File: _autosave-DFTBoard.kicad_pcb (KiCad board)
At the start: 8 copper layers, 120 x 58 mm, 287 parts, among them CON1 AVR-JTAG-10, J1 PJ-102A, J2 AUDIO JACK, J3 AUDIO JACK, J4 AUDIO JACK, J5 JACK_TRS_4PINS, J6 USB_A, J7 USB_B, J8 Micro_SD_Card_Det, J9 HDMI_A, Q1 IRLML2502, Q10 IRLML2502, Q2 IRLML2502, Q3 IRLML2502, Q4 IRLML2502, Q5 IRLML2502, Q6 IRLML2502, Q7 IRLML2502, Q8 IRLML2502, Q9 IRLML2502, SW1 TL6215RF200BDT, U1 LM3880, U10 USB3320, U11 MIC2025-1YMM, U12 USB3320, U13 VL53L0X, U14 APDS-9960, U15 MT41K256M16HA-125_E, U16 MT41K256M16HA-125_E, U17 FTDITypeUART, U18 ABRACON-ASDMB, U19 S25FL256SAGNFI001, U2 LM3880, U20 xc7z020clg484, U22 TSOP344, U3 SC189 - 1.0V, U4 SC189 - 3.3V, U5 TLV62080DSGx, U6 TPS562209DDCT, U7 SC189 - 1.8V, U8 TPS51200DRCR, U9 TLV320AIC3104, Y1 ABM3-24.000MHZ-D2Y-T, Y2 ABM3-24.000MHZ-D2Y-T

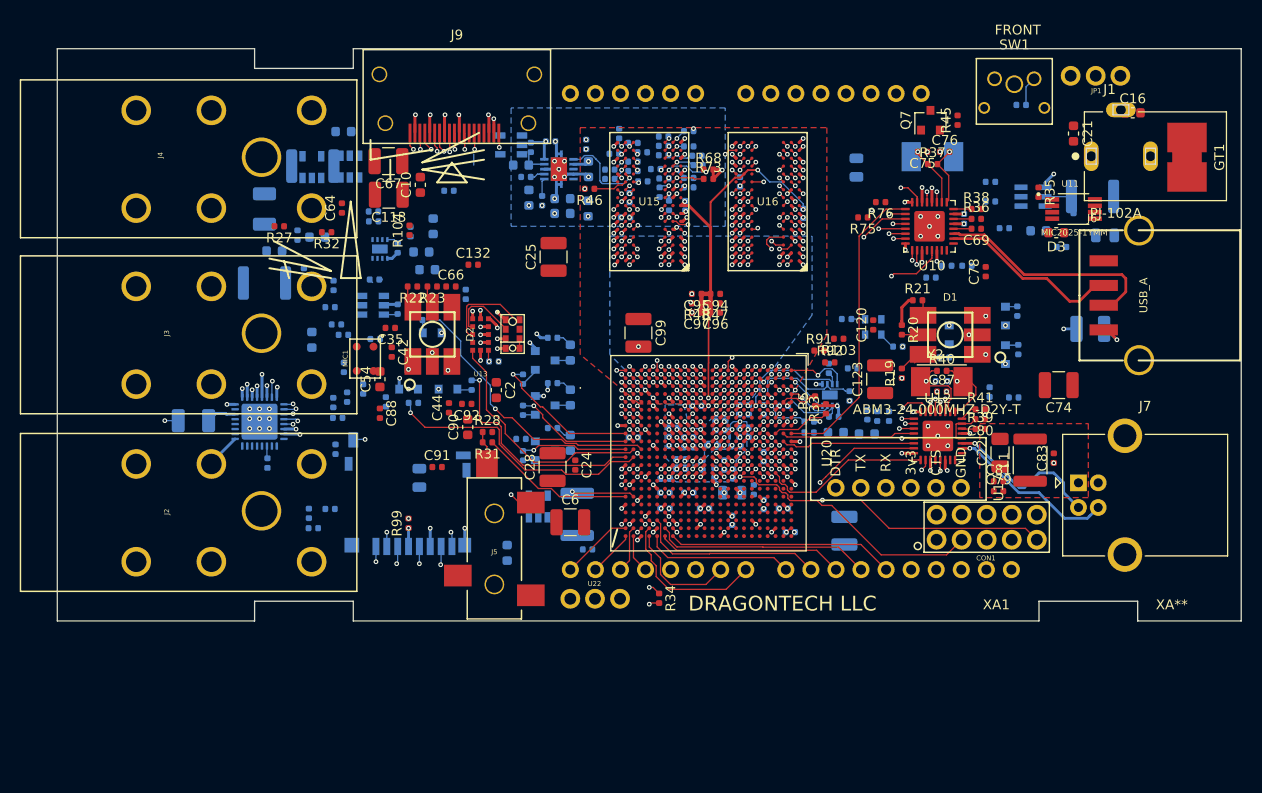
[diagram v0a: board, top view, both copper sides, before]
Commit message: routed a few things, about to remove power jack and 5V regulator
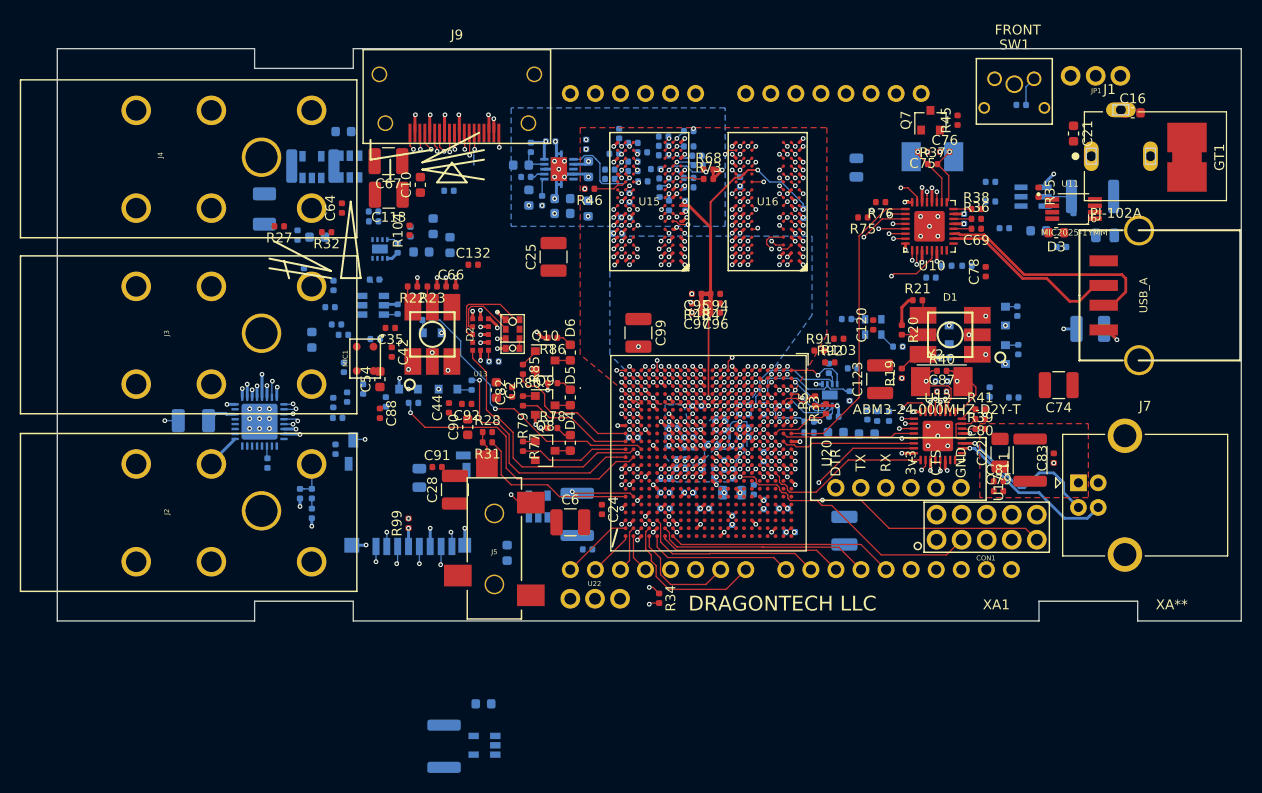
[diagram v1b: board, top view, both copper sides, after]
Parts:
- C82, D4, D5, D6, Q10, Q8, Q9, R77, R78, R79, R80, R85, R86: moved to F.Cu
- moved U7 60.9 mm to (143.3, 170.6)
- moved C26 50.6 mm to (143.2, 166.4)
- moved L4 50.4 mm to (139.2, 170.7), turned to 270 degrees
- moved C102 16.6 mm to (156.8, 118.7), turned to 0 degrees
- moved C28 10.2 mm to (140.3, 144.7)
- moved C24 5.25 mm to (155.2, 146.7)
- moved C82 4.83 mm to (146.1, 134.8), turned to 90 degrees
- moved R17 3.75 mm to (124.6, 145.1), turned to 90 degrees
- moved C41 3.40 mm to (139.8, 119.9), turned to 90 degrees
- moved R18 2.02 mm to (125.8, 145.1)
- moved C36 1.90 mm to (125.8, 147.1), turned to 90 degrees
- moved R85 1.00 mm to (147.2, 132.5), turned to 270 degrees
- moved R79 0.95 mm to (147.2, 135.7), turned to 270 degrees
- moved R77 0.95 mm to (147.2, 140.3), turned to 270 degrees
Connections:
- C36 pad 1: GNDA -> GND
- U20 pad T6: HDMI_CEC -> (no net)
- U20 pad W5: (no net) -> HDMI_CEC
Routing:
- net HDMI_CEC: track 0.00 -> 36.0 mm, vias 0 -> 2
- net /Audio/INSWITCH: track 0.00 -> 3.73 mm
- net GND: track 106.6 -> 110.0 mm, vias 195 -> 198
- net +5V: track 8.42 -> 11.1 mm, vias 6 -> 9
- net JD_HOUT: track 15.8 -> 17.2 mm
- net LED_2R_CTRL: track 27.8 -> 29.2 mm
- net RF_IRQ: track 24.8 -> 26.2 mm
- net LED_2B_CTRL: track 22.9 -> 24.2 mm
- net Net-(R34-Pad1): track 43.4 -> 42.2 mm
- net STATLED_2: track 15.2 -> 14.0 mm, vias 1 -> 0
- net JD_IN: track 0.00 -> 1.03 mm
- net +3V3: track 35.4 -> 36.3 mm, vias 47 -> 48
- net +1V8: track 14.0 -> 14.8 mm, vias 20 -> 21
- net SD_D3: track 62.7 -> 62.1 mm
- net STATLED_0: track 10.8 -> 11.2 mm, vias 1 -> 0
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- added copper zone on SIGNAL4, net +1V0
- added copper zone on SIGNAL4, net +3V3
- added copper zone on SIGNAL1, net GNDA
